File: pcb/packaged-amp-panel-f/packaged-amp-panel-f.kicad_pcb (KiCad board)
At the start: 2 copper layers, 71 x 24.3 mm, 0 parts

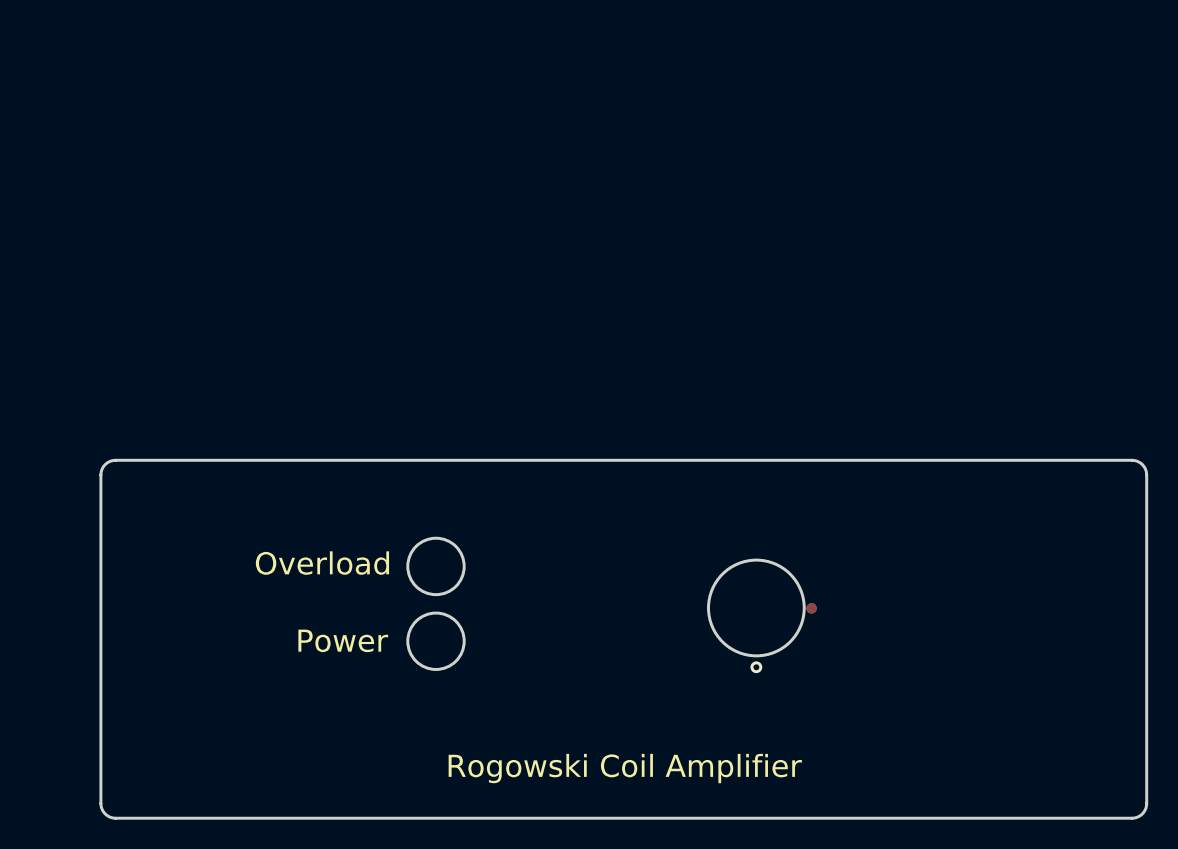
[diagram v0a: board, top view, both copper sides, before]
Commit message: updated panels
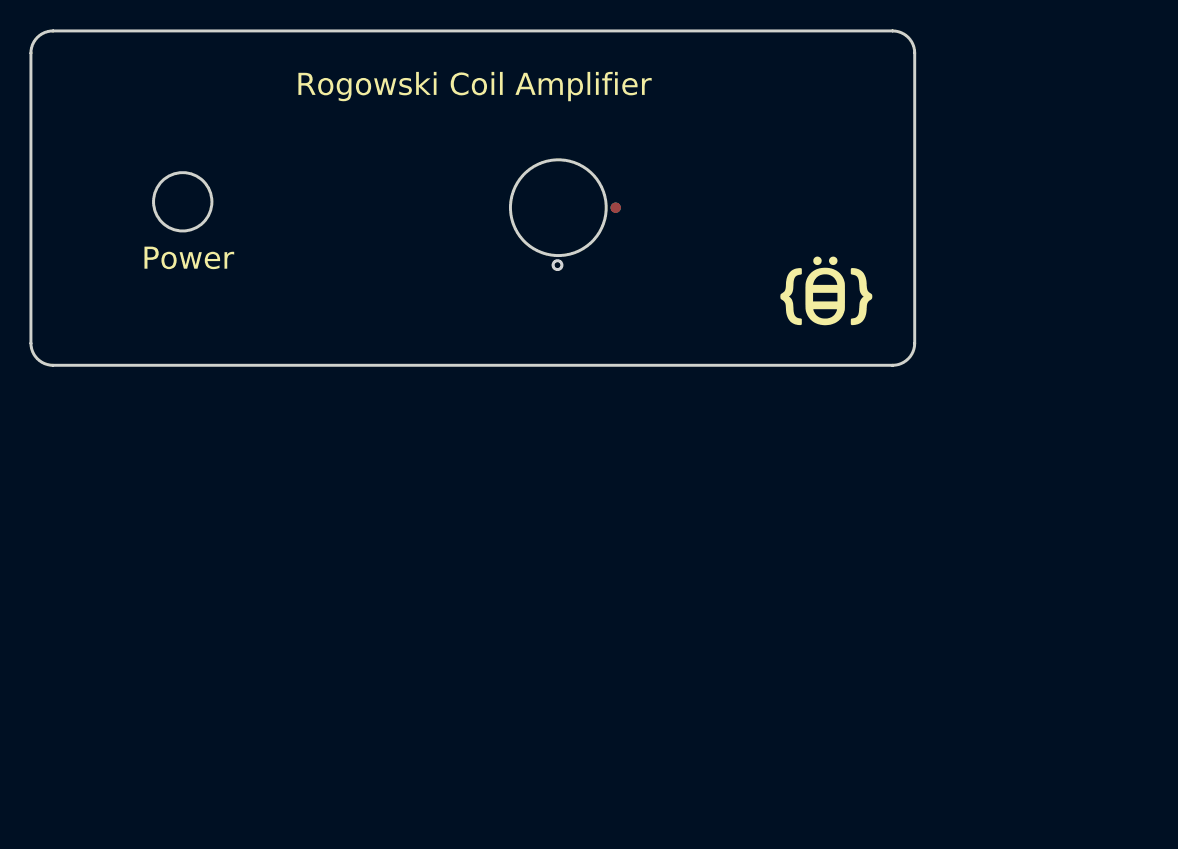
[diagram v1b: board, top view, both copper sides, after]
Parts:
- added G***: LOGO, wbraun_smd:beefield_logo_small, F.Cu at (134.5, 77.3)
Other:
- board size 71 x 24.3 mm -> 60 x 22.7 mm
- board text removed: "Overload"
